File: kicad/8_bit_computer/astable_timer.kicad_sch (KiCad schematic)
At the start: 9 parts, among them U1 NE555P

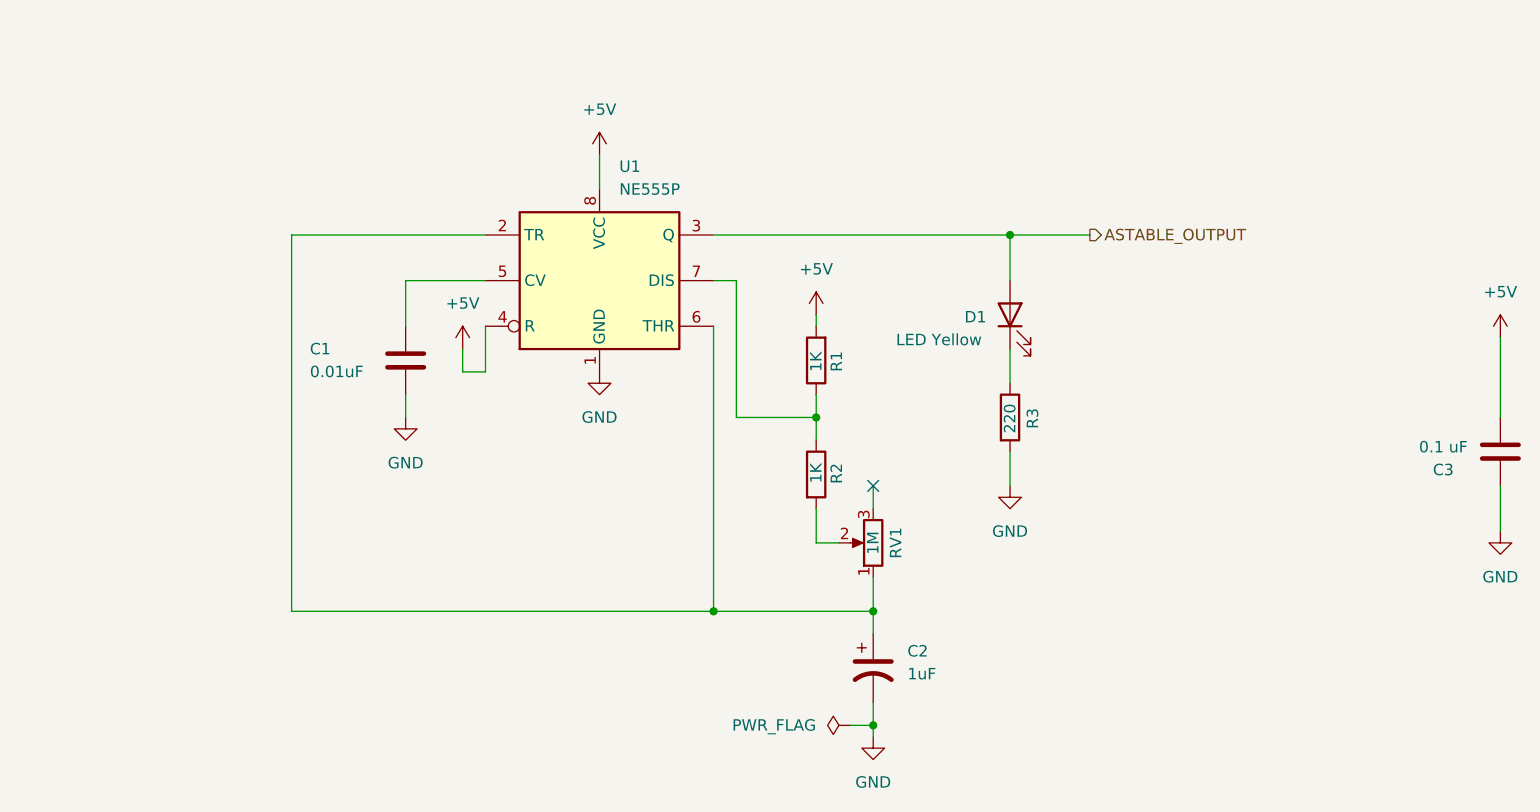
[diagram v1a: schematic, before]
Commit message: Mostly implemented register, still ERC errors
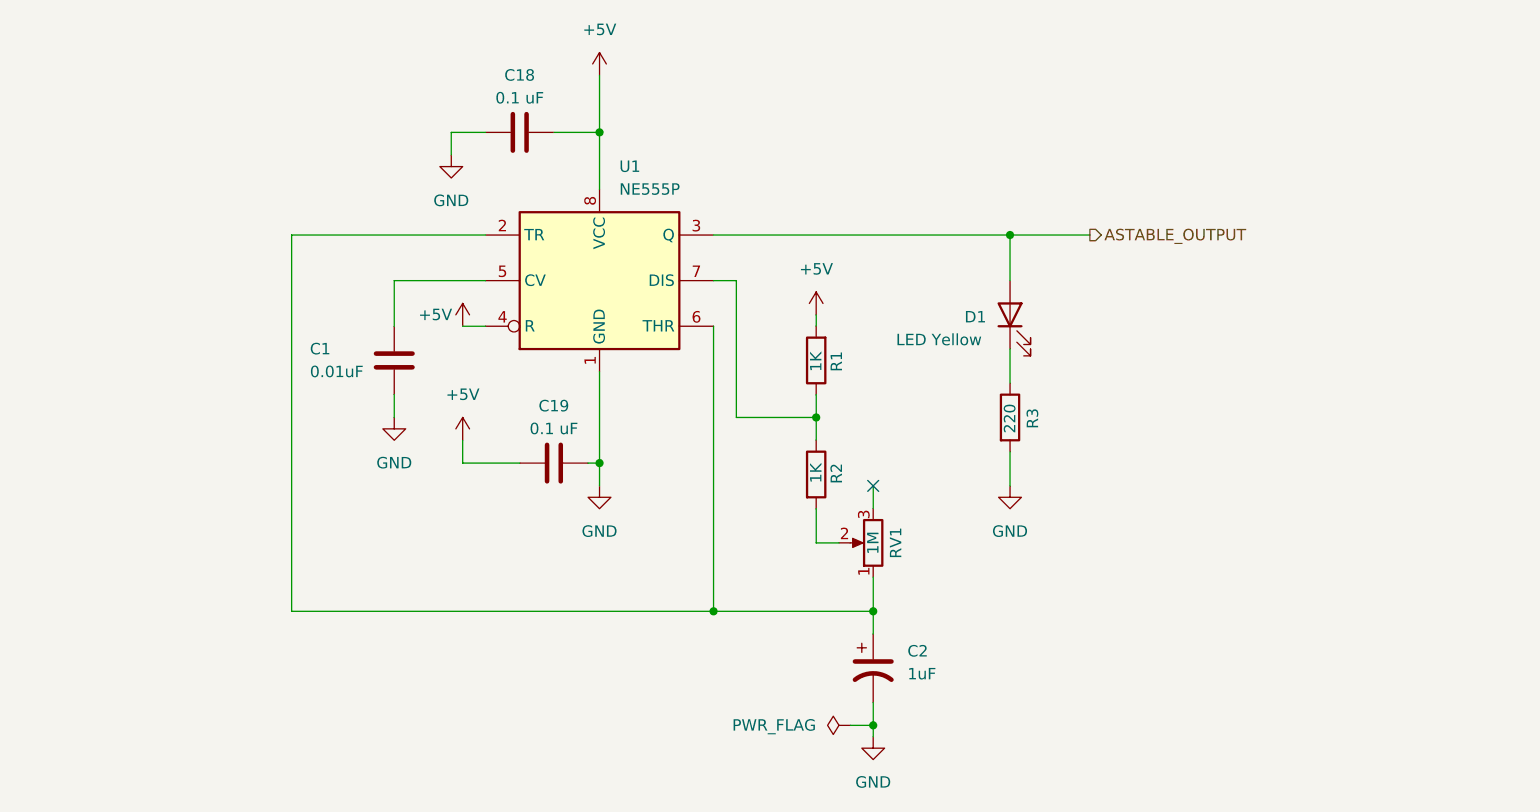
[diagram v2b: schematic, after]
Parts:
- removed C3: 0.1 uF, Capacitor_THT:C_Disc_D5.0mm_W2.5mm_P2.50mm, symbol Device:C
- added C18, C19: 0.1 uF, Capacitor_THT:C_Disc_D5.0mm_W2.5mm_P2.50mm, symbol Device:C
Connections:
- net +5V: now also C18.1, C19.2
- net GND: now also C18.2, C19.1
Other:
- moved on the sheet: C1

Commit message: Add pull up/down resistors to all vcc/gnd shorts
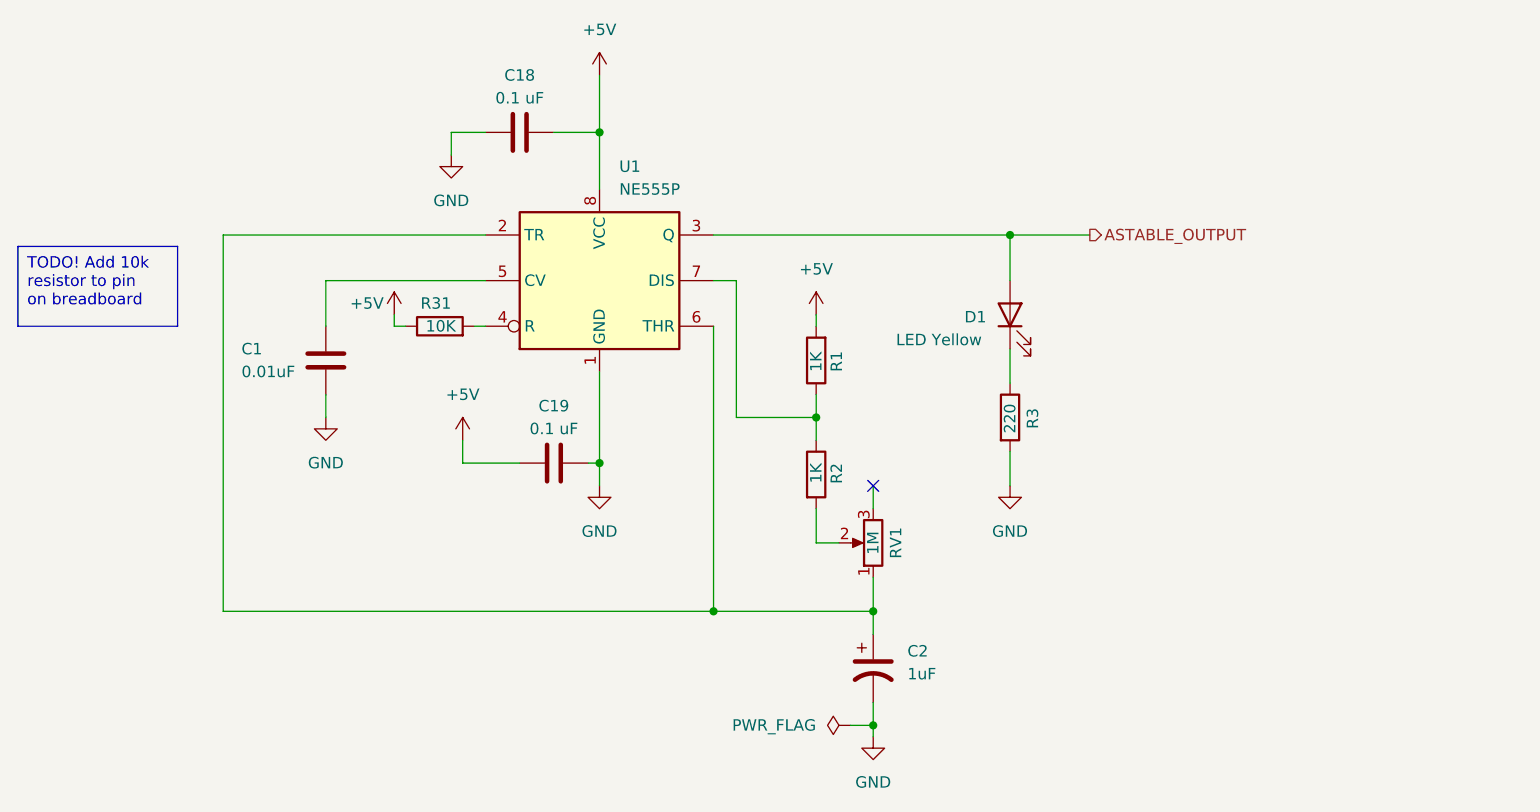
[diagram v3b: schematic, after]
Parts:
- added R31: 10K, Resistor_THT:R_Axial_DIN0207_L6.3mm_D2.5mm_P7.62mm_Horizontal, symbol Device:R
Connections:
- net +5V: now also R31.1; no longer U1.4 (R)
- new net: R31.2, U1.4 (R)
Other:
- moved on the sheet: C1
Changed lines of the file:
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@@
-	(wire
-		(pts
-			(xy 90.17 85.09) (xy 92.71 85.09)
-		)
-		(stroke
-			(width 0)
-			(type default)
-		)
-	)
 	(wire
 		(pts
@@
 	(wire
 		(pts
-			(xy 71.12 74.93) (xy 92.71 74.93)
+			(xy 63.5 74.93) (xy 92.71 74.93)
 		)
 		(stroke
@@
 	(wire
 		(pts
-			(xy 71.12 116.84) (xy 118.11 116.84)
+			(xy 63.5 116.84) (xy 118.11 116.84)
 		)
 		(stroke
@@
 	(wire
 		(pts
+			(xy 82.55 85.09) (xy 83.82 85.09)
+		)
+		(stroke
+			(width 0)
+			(type default)
+		)
+	)
+	(wire
+		(pts
 			(xy 105.41 57.15) (xy 105.41 63.5)
 		)
@@
 	(wire
 		(pts
-			(xy 71.12 74.93) (xy 71.12 116.84)
-		)
-		(stroke
-			(width 0)
-			(type default)
-		)
-	)
-	(wire
-		(pts
-			(xy 92.71 80.01) (xy 82.55 80.01)
+			(xy 63.5 74.93) (xy 63.5 116.84)
+		)
+		(stroke
+			(width 0)
+			(type default)
+		)
+	)
+	(wire
+		(pts
+			(xy 92.71 80.01) (xy 74.93 80.01)
 		)
 		(stroke
@@
 	(wire
 		(pts
-			(xy 82.55 92.71) (xy 82.55 95.25)
-		)
-		(stroke
-			(width 0)
-			(type default)
-		)
-	)
-	(wire
-		(pts
-			(xy 82.55 80.01) (xy 82.55 85.09)
+			(xy 91.44 85.09) (xy 92.71 85.09)
+		)
+		(stroke
+			(width 0)
+			(type default)
+		)
+	)
+	(wire
+		(pts
+			(xy 82.55 83.82) (xy 82.55 85.09)
+		)
+		(stroke
+			(width 0)
+			(type default)
+		)
+	)
+	(wire
+		(pts
+			(xy 74.93 92.71) (xy 74.93 95.25)
+		)
+		(stroke
+			(width 0)
+			(type default)
+		)
+	)
+	(wire
+		(pts
+			(xy 74.93 80.01) (xy 74.93 85.09)
 		)
 		(stroke
@@
 			(width 0)
 			(type default)
+		)
+	)
+	(text_box "TODO! Add 10k resistor to pin on breadboard"
+		(exclude_from_sim no)
+		(at 40.64 76.2 0)
+		(size 17.78 8.89)
+		(stroke
+			(width 0)
+			(type default)
+		)
+		(fill
+			(type none)
+		)
+		(effects
+			(font
+				(size 1.27 1.27)
+			)
+			(justify left top)
 		)
 	)
@@
 	(symbol
 		(lib_id "power:GND")
-		(at 82.55 95.25 0)
+		(at 74.93 95.25 0)
 		(unit 1)
 		(exclude_from_sim no)
@@
 		(fields_autoplaced yes)
 		(property "Reference" "#PWR011"
-			(at 82.55 101.6 0)
+			(at 74.93 101.6 0)
 			(effects
 				(font
@@
 		)
 		(property "Value" "GND"
-			(at 82.55 100.33 0)
+			(at 74.93 100.33 0)
 			(effects
 				(font
@@
 		)
 		(property "Footprint" ""
-			(at 82.55 95.25 0)
+			(at 74.93 95.25 0)
 			(effects
 				(font
@@
 		)
 		(property "Datasheet" ""
-			(at 82.55 95.25 0)
+			(at 74.93 95.25 0)
 			(effects
 				(font
@@
 		)
 		(property "Description" "Power symbol creates a global label with name \"GND\" , ground"
-			(at 82.55 95.25 0)
+			(at 74.93 95.25 0)
 			(effects
 				(font
@@
 	(symbol
 		(lib_id "power:+5V")
-		(at 90.17 85.09 0)
+		(at 82.55 83.82 0)
 		(unit 1)
 		(exclude_from_sim no)
@@
 		(dnp no)
 		(property "Reference" "#PWR013"
-			(at 90.17 88.9 0)
+			(at 82.55 87.63 0)
 			(effects
 				(font
@@
 		)
 		(property "Value" "+5V"
-			(at 87.122 83.82 0)
+			(at 79.502 82.55 0)
 			(effects
 				(font
@@
 		)
 		(property "Footprint" ""
-			(at 90.17 85.09 0)
+			(at 82.55 83.82 0)
 			(effects
 				(font
@@
 		)
 		(property "Datasheet" ""
-			(at 90.17 85.09 0)
+			(at 82.55 83.82 0)
 			(effects
 				(font
@@
 		)
 		(property "Description" "Power symbol creates a global label with name \"+5V\""
-			(at 90.17 85.09 0)
+			(at 82.55 83.82 0)
 			(effects
 				(font
@@
 	(symbol
 		(lib_id "Device:C")
-		(at 82.55 88.9 0)
+		(at 74.93 88.9 0)
 		(unit 1)
 		(exclude_from_sim no)
@@
 		(dnp no)
 		(property "Reference" "C1"
-			(at 73.152 87.63 0)
+			(at 65.532 87.63 0)
 			(effects
 				(font
@@
 		)
 		(property "Value" "0.01uF"
-			(at 73.152 90.17 0)
+			(at 65.532 90.17 0)
 			(effects
 				(font
@@
 		)
 		(property "Footprint" "Capacitor_THT:C_Disc_D5.0mm_W2.5mm_P2.50mm"
-			(at 83.5152 92.71 0)
+			(at 75.8952 92.71 0)
 			(effects
 				(font
@@
 		)
 		(property "Datasheet" "https://www.vishay.com/docs/45171/kseries.pdf"
-			(at 82.55 88.9 0)
+			(at 74.93 88.9 0)
 			(effects
 				(font
@@
 		)
 		(property "Description" "Unpolarized capacitor."
-			(at 82.55 88.9 0)
+			(at 74.93 88.9 0)
 			(effects
 				(font
@@
 		)
 		(property "Manufacturer PN" "K103M15X7RF53L2"
-			(at 82.55 88.9 0)
+			(at 74.93 88.9 0)
 			(effects
 				(font
@@
 		)
 		(property "Digkey PN" " BC5136-ND"
-			(at 82.55 88.9 0)
+			(at 74.93 88.9 0)
 			(effects
 				(font
@@
 		)
 		(property "DigiKey URL" "https://www.digikey.com/en/products/detail/vishay-beyschlag-draloric-bc-components/K103M15X7RF53L2/2820467"
-			(at 82.55 88.9 0)
+			(at 74.93 88.9 0)
 			(effects
 				(font
@@
 		)
 		(property "Price" "0.16"
-			(at 82.55 88.9 0)
+			(at 74.93 88.9 0)
 			(effects
 				(font
@@
 		)
 		(property "DigiKey PN" ""
-			(at 82.55 88.9 0)
+			(at 74.93 88.9 0)
 			(effects
 				(font
@@
 					(unit 1)
 				)
+			)
+		)
+	)
+	(symbol
+		(lib_id "Device:R")
+		(at 87.63 85.09 90)
+		(unit 1)
+		(exclude_from_sim no)
+		(in_bom yes)
+		(on_board yes)
+		(dnp no)
+		(property "Reference" "R31"
+			(at 88.9 82.55 90)
+			(effects
+				(font
+					(size 1.27 1.27)
+				)
+				(justify left)
+			)
+		)
+		(property "Value" "10K"
+			(at 89.408 85.09 90)
+			(effects
+				(font
+					(size 1.27 1.27)
+				)
+				(justify left)
+			)
+		)
+		(property "Footprint" "Resistor_THT:R_Axial_DIN0207_L6.3mm_D2.5mm_P7.62mm_Horizontal"
+			(at 87.63 86.868 90)
+			(effects
+				(font
+					(size 1.27 1.27)
+				)
+				(hide yes)
+			)
+		)
+		(property "Datasheet" "https://www.yageo.com/upload/media/product/app/datasheet/lr/yageo-mfr_datasheet.pdf"
+			(at 87.63 85.09 0)
+			(effects
+				(font
+					(size 1.27 1.27)
+				)
+				(hide yes)
+			)
+		)
+		(property "Description" "Resistor"
+			(at 87.63 85.09 0)
+			(effects
+				(font
+					(size 1.27 1.27)
+				)
+				(hide yes)
+			)
+		)
+		(property "Digkey PN" "13-MFR-25FRF52-10KCT-ND "
+			(at 87.63 85.09 0)
+			(effects
+				(font
+					(size 1.27 1.27)
+				)
+				(hide yes)
+			)
+		)
+		(property "Manufacturer PN" "MFR-25FRF52-10K"
+			(at 87.63 85.09 0)
+			(effects
+				(font
+					(size 1.27 1.27)
+				)
+				(hide yes)
+			)
+		)
+		(property "DigiKey URL" "https://www.digikey.com/en/products/detail/yageo/MFR-25FRF52-10K/14626"
+			(at 87.63 85.09 0)
+			(effects
+				(font
+					(size 1.27 1.27)
+				)
+				(hide yes)
+			)
+		)
+		(property "Price" "0.10"
+			(at 87.63 85.09 0)
+			(effects
+				(font
+					(size 1.27 1.27)
+				)
+				(hide yes)
+			)
+		)
+		(property "DigiKey PN" ""
+			(at 87.63 85.09 0)
+			(effects
+				(font
+					(size 1.27 1.27)
+				)
+				(hide yes)
+			)
+		)
+		(pin "2"
+		)
+		(pin "1"
+		)
+		(instances
+			(project "8_bit_computer"
+				(path "/24dbb59b-fc31-4588-b2ee-d18f20639e07/62eb35ce-6b42-428c-8bc5-4f1b242b0bef/2b1e6d59-b5a1-4cb0-9534-b2be7027a28c"
+					(reference "R31")
+					(unit 1)
+				)
